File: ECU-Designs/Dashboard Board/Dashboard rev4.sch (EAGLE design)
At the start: 23 parts, among them U1 SN65HVD230D

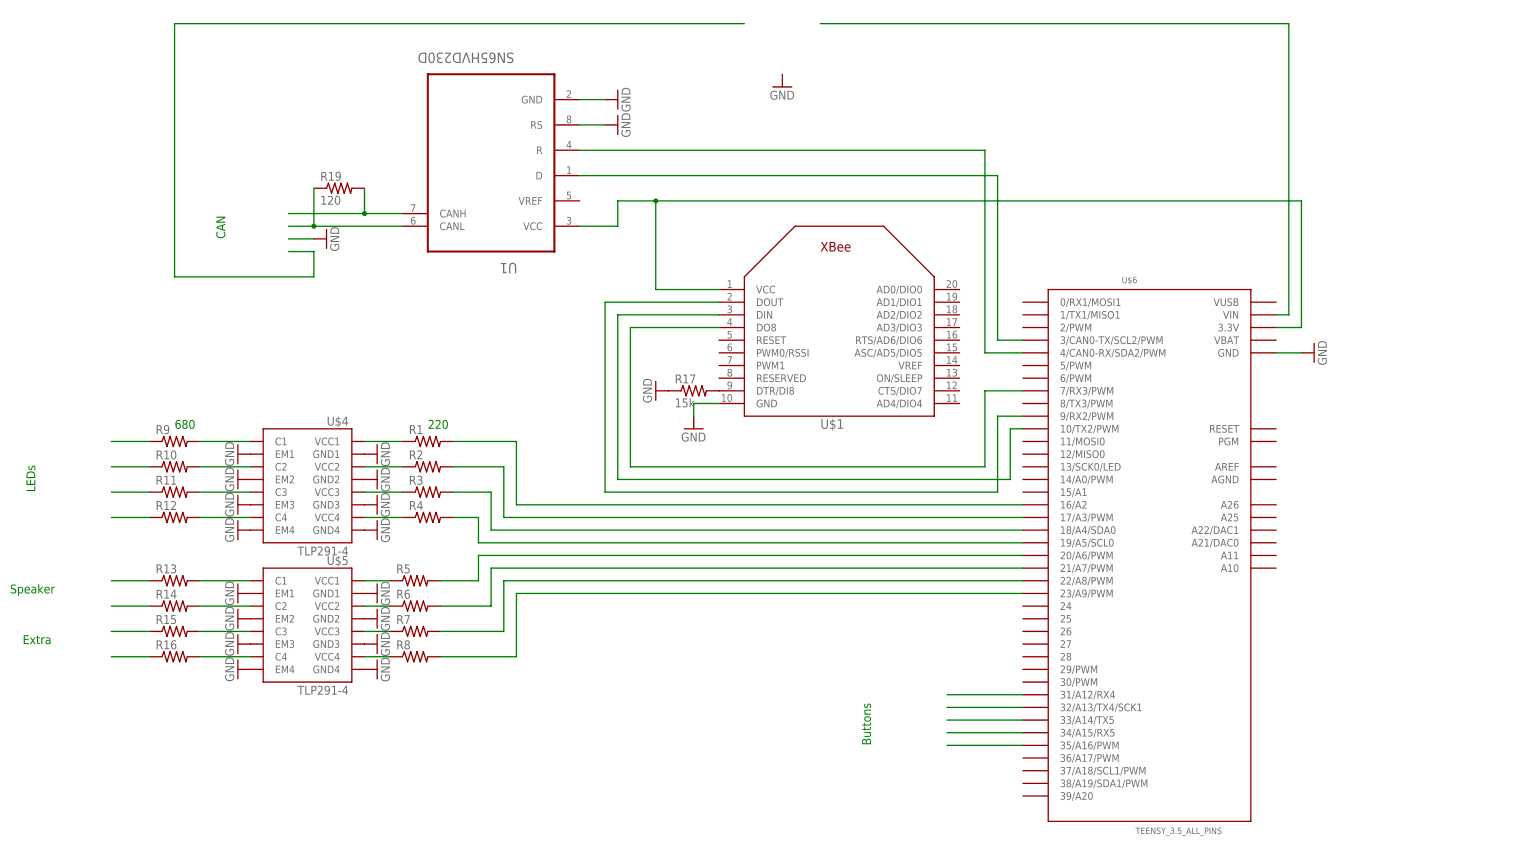
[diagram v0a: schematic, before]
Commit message: Updated dashboard
Dashboard rev4 board and schematic
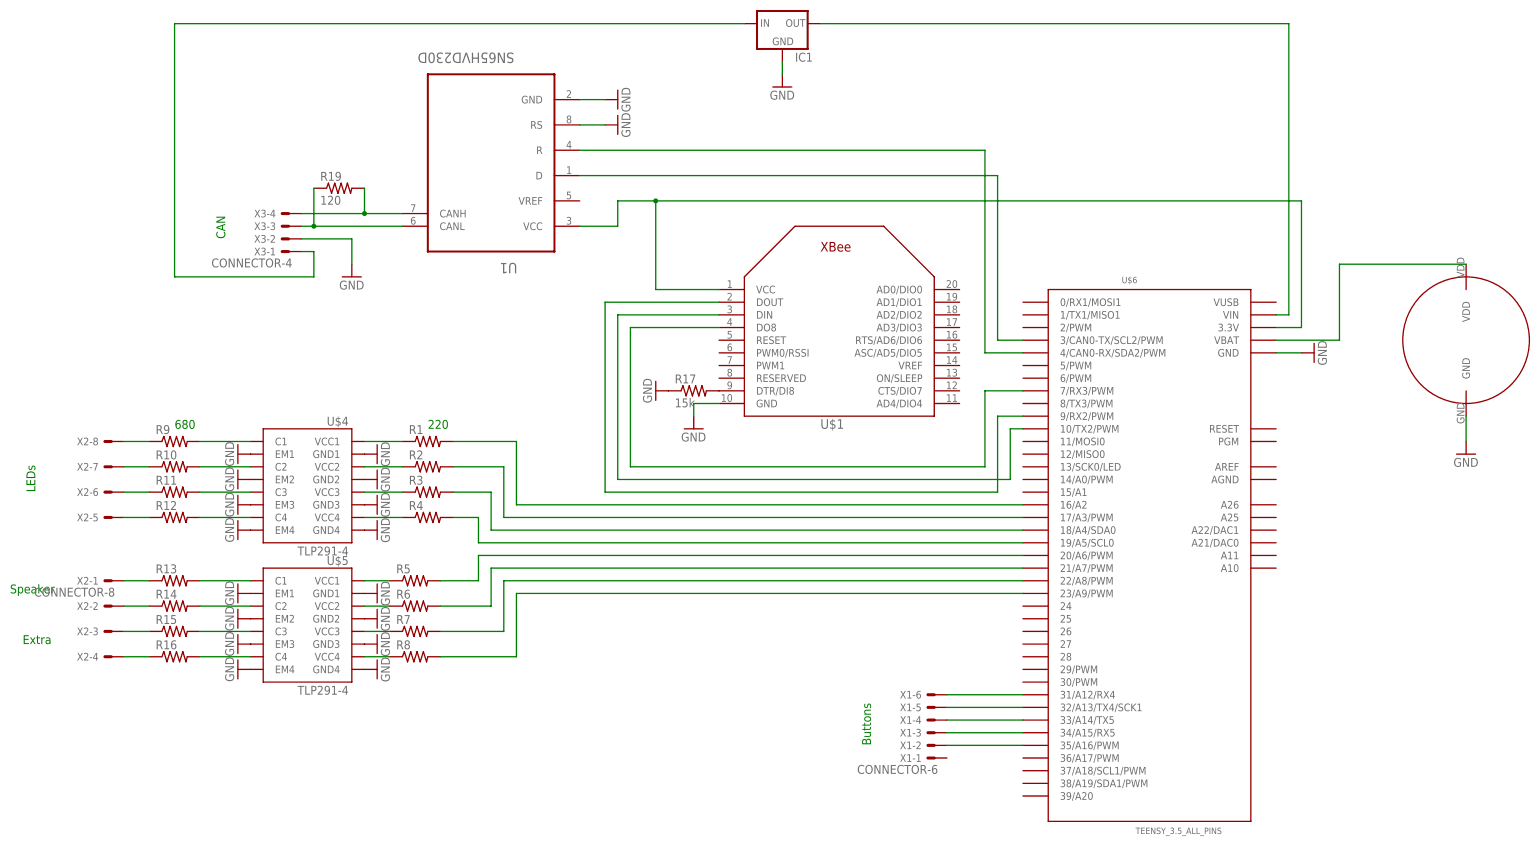
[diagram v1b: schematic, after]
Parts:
- added IC1: (no value), HyTechDevices2:5VREG_L7805SPACED
- added U$2: COIN-CELL-HOLDER, HyTechDevices2:COIN-CELL-HOLDER
- added X1: CONNECTOR-6, HyTechDevices2:CONNECTOR-6
- added X2: CONNECTOR-8, HyTechDevices2:CONNECTOR-8
- added X3: CONNECTOR-4, HyTechDevices2:CONNECTOR-4
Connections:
- new net N$23: U$2.VDD, U$6.VBAT
- new net N$43: IC1.IN, X3-1.S
- net GND: now also IC1.GND, U$2.GND, X3-2.S
- net N$1: now also X2-8.S
- net N$17: now also X1-6.S
- net N$18: now also X2-1.S
- net N$19: now also X1-5.S
- net N$20: now also X1-4.S
- net N$21: now also X1-3.S
- net N$22: now also X1-2.S
- net N$3: now also X2-7.S
- net N$33: now also X2-2.S
- net N$34: now also X2-3.S
- net N$35: now also X2-4.S
- net N$37: now also X3-4.S
- net N$4: now also X2-6.S
- net N$41: now also X3-3.S
- net N$42: now also IC1.OUT
- net N$6: now also X2-5.S
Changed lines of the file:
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@@
 <part name="R17" library="HyTechDevices" deviceset="RESISTOR" device="AXIAL-0.3" value="15k"/>
 <part name="GND23" library="HyTechSymbols" deviceset="GND" device=""/>
+<part name="U$2" library="HyTechDevices2" deviceset="COIN-CELL-HOLDER" device=""/>
+<part name="X1" library="HyTechDevices2" deviceset="CONNECTOR-6" device=""/>
+<part name="X2" library="HyTechDevices2" deviceset="CONNECTOR-8" device=""/>
+<part name="X3" library="HyTechDevices2" deviceset="CONNECTOR-4" device=""/>
+<part name="IC1" library="HyTechDevices2" deviceset="5VREG_L7805" device="SPACED"/>
+<part name="GND24" library="HyTechSymbols" deviceset="GND" device=""/>
 </parts>
 <sheets>
@@
 <instance part="GND17" gate="1" x="-73.66" y="147.32" rot="R90"/>
 <instance part="GND18" gate="1" x="-73.66" y="142.24" rot="R90"/>
-<instance part="GND19" gate="1" x="-132.08" y="119.38" rot="R90"/>
+<instance part="GND19" gate="1" x="-127" y="111.76"/>
 <instance part="GND20" gate="1" x="-40.64" y="149.86"/>
 <instance part="R19" gate="G$1" x="-129.54" y="129.54"/>
@@
 <instance part="R17" gate="G$1" x="-58.42" y="88.9"/>
 <instance part="GND23" gate="1" x="66.04" y="96.52" rot="R90"/>
+<instance part="U$2" gate="G$1" x="96.52" y="99.06" rot="R270"/>
+<instance part="X1" gate="-1" x="-10.16" y="15.24" rot="R180"/>
+<instance part="X1" gate="-2" x="-10.16" y="17.78" rot="R180"/>
+<instance part="X1" gate="-3" x="-10.16" y="20.32" rot="R180"/>
+<instance part="X1" gate="-4" x="-10.16" y="22.86" rot="R180"/>
+<instance part="X1" gate="-5" x="-10.16" y="25.4" rot="R180"/>
+<instance part="X1" gate="-6" x="-10.16" y="27.94" rot="R180"/>
+<instance part="X2" gate="-1" x="-175.26" y="50.8" rot="R180"/>
+<instance part="X2" gate="-2" x="-175.26" y="45.72" rot="R180"/>
+<instance part="X2" gate="-3" x="-175.26" y="40.64" rot="R180"/>
+<instance part="X2" gate="-4" x="-175.26" y="35.56" rot="R180"/>
+<instance part="X2" gate="-5" x="-175.26" y="63.5" rot="R180"/>
+<instance part="X2" gate="-6" x="-175.26" y="68.58" rot="R180"/>
+<instance part="X2" gate="-7" x="-175.26" y="73.66" rot="R180"/>
+<instance part="X2" gate="-8" x="-175.26" y="78.74" rot="R180"/>
+<instance part="X3" gate="-1" x="-139.7" y="116.84" rot="R180"/>
+<instance part="X3" gate="-2" x="-139.7" y="119.38" rot="R180"/>
+<instance part="X3" gate="-3" x="-139.7" y="121.92" rot="R180"/>
+<instance part="X3" gate="-4" x="-139.7" y="124.46" rot="R180"/>
+<instance part="IC1" gate="G$1" x="-40.64" y="162.56"/>
+<instance part="GND24" gate="1" x="96.52" y="76.2"/>
 </instances>
 <busses>
@@
 </segment>
 <segment>
-<pinref part="GND19" gate="1" pin="GND"/>
-<wire x1="-139.7" y1="119.38" x2="-134.62" y2="119.38" width="0.1524" layer="91"/>
-</segment>
-<segment>
 <pinref part="GND21" gate="1" pin="GND"/>
 <wire x1="-58.42" y1="83.82" x2="-58.42" y2="86.36" width="0.1524" layer="91"/>
@@
 <pinref part="GND23" gate="1" pin="GND"/>
 <wire x1="63.5" y1="96.52" x2="58.42" y2="96.52" width="0.1524" layer="91"/>
+</segment>
+<segment>
+<pinref part="IC1" gate="G$1" pin="GND"/>
+<pinref part="GND20" gate="1" pin="GND"/>
+<wire x1="-40.64" y1="154.94" x2="-40.64" y2="152.4" width="0.1524" layer="91"/>
+</segment>
+<segment>
+<pinref part="X3" gate="-2" pin="S"/>
+<pinref part="GND19" gate="1" pin="GND"/>
+<wire x1="-137.16" y1="119.38" x2="-127" y2="119.38" width="0.1524" layer="91"/>
+<wire x1="-127" y1="119.38" x2="-127" y2="114.3" width="0.1524" layer="91"/>
+</segment>
+<segment>
+<pinref part="U$2" gate="G$1" pin="GND"/>
+<pinref part="GND24" gate="1" pin="GND"/>
+<wire x1="96.52" y1="83.82" x2="96.52" y2="78.74" width="0.1524" layer="91"/>
 </segment>
 </net>
@@
 <segment>
 <pinref part="R9" gate="G$1" pin="1"/>
-<wire x1="-175.26" y1="78.74" x2="-167.64" y2="78.74" width="0.1524" layer="91"/>
+<wire x1="-172.72" y1="78.74" x2="-167.64" y2="78.74" width="0.1524" layer="91"/>
+<pinref part="X2" gate="-8" pin="S"/>
 </segment>
 </net>
@@
 <segment>
 <pinref part="R10" gate="G$1" pin="1"/>
-<wire x1="-175.26" y1="73.66" x2="-167.64" y2="73.66" width="0.1524" layer="91"/>
+<wire x1="-172.72" y1="73.66" x2="-167.64" y2="73.66" width="0.1524" layer="91"/>
+<pinref part="X2" gate="-7" pin="S"/>
 </segment>
 </net>
@@
 <segment>
 <pinref part="R11" gate="G$1" pin="1"/>
-<wire x1="-175.26" y1="68.58" x2="-167.64" y2="68.58" width="0.1524" layer="91"/>
+<wire x1="-172.72" y1="68.58" x2="-167.64" y2="68.58" width="0.1524" layer="91"/>
+<pinref part="X2" gate="-6" pin="S"/>
 </segment>
 </net>
@@
 <segment>
 <pinref part="R12" gate="G$1" pin="1"/>
-<wire x1="-175.26" y1="63.5" x2="-167.64" y2="63.5" width="0.1524" layer="91"/>
-</segment>
-</net>
-<net name="N$18" class="0">
-<segment>
-<pinref part="R13" gate="G$1" pin="1"/>
-<wire x1="-175.26" y1="50.8" x2="-167.64" y2="50.8" width="0.1524" layer="91"/>
-</segment>
-</net>
-<net name="N$33" class="0">
-<segment>
-<pinref part="R14" gate="G$1" pin="1"/>
-<wire x1="-175.26" y1="45.72" x2="-167.64" y2="45.72" width="0.1524" layer="91"/>
-</segment>
-</net>
-<net name="N$34" class="0">
-<segment>
-<pinref part="R15" gate="G$1" pin="1"/>
-<wire x1="-175.26" y1="40.64" x2="-167.64" y2="40.64" width="0.1524" layer="91"/>
-</segment>
-</net>
-<net name="N$35" class="0">
-<segment>
-<pinref part="R16" gate="G$1" pin="1"/>
-<wire x1="-175.26" y1="35.56" x2="-167.64" y2="35.56" width="0.1524" layer="91"/>
+<wire x1="-172.72" y1="63.5" x2="-167.64" y2="63.5" width="0.1524" layer="91"/>
+<pinref part="X2" gate="-5" pin="S"/>
 </segment>
 </net>
@@
 <pinref part="U$6" gate="G$1" pin="31/A12/RX4"/>
 <wire x1="-7.62" y1="27.94" x2="7.62" y2="27.94" width="0.1524" layer="91"/>
+<pinref part="X1" gate="-6" pin="S"/>
 </segment>
 </net>
@@
 <pinref part="U$6" gate="G$1" pin="32/A13/TX4/SCK1"/>
 <wire x1="-7.62" y1="25.4" x2="7.62" y2="25.4" width="0.1524" layer="91"/>
+<pinref part="X1" gate="-5" pin="S"/>
 </segment>
 </net>
@@
 <pinref part="U$6" gate="G$1" pin="33/A14/TX5"/>
 <wire x1="-7.62" y1="22.86" x2="7.62" y2="22.86" width="0.1524" layer="91"/>
+<pinref part="X1" gate="-4" pin="S"/>
 </segment>
 </net>
@@
 <pinref part="U$6" gate="G$1" pin="34/A15/RX5"/>
 <wire x1="-7.62" y1="20.32" x2="7.62" y2="20.32" width="0.1524" layer="91"/>
+<pinref part="X1" gate="-3" pin="S"/>
 </segment>
 </net>
@@
 <pinref part="U$6" gate="G$1" pin="35/A16/PWM"/>
 <wire x1="-7.62" y1="17.78" x2="7.62" y2="17.78" width="0.1524" layer="91"/>
+<pinref part="X1" gate="-2" pin="S"/>
 </segment>
 </net>
@@
 <segment>
 <pinref part="U1" gate="A" pin="CANH"/>
-<wire x1="-139.7" y1="124.46" x2="-124.46" y2="124.46" width="0.1524" layer="91"/>
+<wire x1="-137.16" y1="124.46" x2="-124.46" y2="124.46" width="0.1524" layer="91"/>
 <pinref part="R19" gate="G$1" pin="2"/>
 <wire x1="-124.46" y1="124.46" x2="-116.84" y2="124.46" width="0.1524" layer="91"/>
 <wire x1="-124.46" y1="124.46" x2="-124.46" y2="129.54" width="0.1524" layer="91"/>
 <junction x="-124.46" y="124.46"/>
+<pinref part="X3" gate="-4" pin="S"/>
 </segment>
 </net>
@@
 <wire x1="-116.84" y1="121.92" x2="-134.62" y2="121.92" width="0.1524" layer="91"/>
 <pinref part="R19" gate="G$1" pin="1"/>
-<wire x1="-134.62" y1="121.92" x2="-139.7" y2="121.92" width="0.1524" layer="91"/>
+<wire x1="-134.62" y1="121.92" x2="-137.16" y2="121.92" width="0.1524" layer="91"/>
 <wire x1="-134.62" y1="129.54" x2="-134.62" y2="121.92" width="0.1524" layer="91"/>
 <junction x="-134.62" y="121.92"/>
+<pinref part="X3" gate="-3" pin="S"/>
 </segment>
 </net>
 <net name="N$43" class="0">
 <segment>
-<wire x1="-139.7" y1="116.84" x2="-134.62" y2="116.84" width="0.1524" layer="91"/>
+<wire x1="-137.16" y1="116.84" x2="-134.62" y2="116.84" width="0.1524" layer="91"/>
 <wire x1="-134.62" y1="116.84" x2="-134.62" y2="111.76" width="0.1524" layer="91"/>
 <wire x1="-134.62" y1="111.76" x2="-162.56" y2="111.76" width="0.1524" layer="91"/>
 <wire x1="-162.56" y1="111.76" x2="-162.56" y2="162.56" width="0.1524" layer="91"/>
 <wire x1="-162.56" y1="162.56" x2="-48.26" y2="162.56" width="0.1524" layer="91"/>
+<pinref part="X3" gate="-1" pin="S"/>
+<pinref part="IC1" gate="G$1" pin="IN"/>
 </segment>
 </net>
@@
 <pinref part="U$6" gate="G$1" pin="VIN"/>
 <wire x1="60.96" y1="104.14" x2="58.42" y2="104.14" width="0.1524" layer="91"/>
+<pinref part="IC1" gate="G$1" pin="OUT"/>
 </segment>
 </net>
@@
 </segment>
 </net>
+<net name="N$23" class="0">
+<segment>
+<pinref part="U$2" gate="G$1" pin="VDD"/>
+<wire x1="96.52" y1="114.3" x2="71.12" y2="114.3" width="0.1524" layer="91"/>
+<wire x1="71.12" y1="114.3" x2="71.12" y2="99.06" width="0.1524" layer="91"/>
+<pinref part="U$6" gate="G$1" pin="VBAT"/>
+<wire x1="71.12" y1="99.06" x2="58.42" y2="99.06" width="0.1524" layer="91"/>
+</segment>
+</net>
+<net name="N$18" class="0">
+<segment>
+<pinref part="R13" gate="G$1" pin="1"/>
+<pinref part="X2" gate="-1" pin="S"/>
+<wire x1="-172.72" y1="50.8" x2="-167.64" y2="50.8" width="0.1524" layer="91"/>
+</segment>
+</net>
+<net name="N$33" class="0">
+<segment>
+<pinref part="R14" gate="G$1" pin="1"/>
+<pinref part="X2" gate="-2" pin="S"/>
+<wire x1="-172.72" y1="45.72" x2="-167.64" y2="45.72" width="0.1524" layer="91"/>
+</segment>
+</net>
+<net name="N$34" class="0">
+<segment>
+<pinref part="R15" gate="G$1" pin="1"/>
+<pinref part="X2" gate="-3" pin="S"/>
+<wire x1="-172.72" y1="40.64" x2="-167.64" y2="40.64" width="0.1524" layer="91"/>
+</segment>
+</net>
+<net name="N$35" class="0">
+<segment>
+<pinref part="R16" gate="G$1" pin="1"/>
+<pinref part="X2" gate="-4" pin="S"/>
+<wire x1="-172.72" y1="35.56" x2="-167.64" y2="35.56" width="0.1524" layer="91"/>
+</segment>
+</net>
